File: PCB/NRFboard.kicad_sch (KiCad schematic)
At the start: 39 parts, among them J1 USB_C_Receptacle_USB2.0_14P, J2 Conn_01x20, J3 Conn_01x20, J4 Conn_01x03, J5 Conn_01x03, SW1 SW_Push, U2 MCP1700x-300xxTT, U4 nRF52840, U7 BQ24075RGT, Y1 32Mhz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

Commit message: updated routing, should be finalized and ready for production
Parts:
- added C10, C9: 10uF, Capacitor_SMD:C_0603_1608Metric, symbol Device:C
- added C11, C5: 1uF, Capacitor_SMD:C_0402_1005Metric, symbol Device:C
- added C4, C8: 0.1uF, Capacitor_SMD:C_0402_1005Metric, symbol Device:C
- added C6: 22uF, Capacitor_SMD:C_0805_2012Metric, symbol Device:C
- added D1: green, LED_SMD:LED_0805_2012Metric, symbol Device:LED
- added J6: Conn_01x02, Connector_JST:JST_PH_B2B-PH-K_1x02_P2.00mm_Vertical, symbol Connector_Generic:Conn_01x02
- added R4: 1.5k, Resistor_SMD:R_0402_1005Metric, symbol Device:R
- C18, C19: value 20pF -> 12pF
- C22, C25, C29: footprint Capacitor_SMD:C_0402_1005Metric -> Capacitor_SMD:C_0603_1608Metric
- C31, C32: value 15pF -> 12.5pF
- R11: value 10k -> 1.5k
- renumbered D89 to D2
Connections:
- net +3V3: now also C11.1, C9.1
- net GND: now also U7.6 (EN1), C10.1, C11.2, C4.2, C5.2, C6.2, C8.2, C9.2, J6.2 (Pin_2); no longer U7.5 (EN2)
- net Out: now also J3.20 (Pin_20), C10.2, C4.1, C5.1, C6.1, C8.1, R4.2
- net VBAT: now also U7.5 (EN2), J6.1 (Pin_1); no longer J3.20 (Pin_20), U7.6 (EN1)
- net at U7.7 (~{PGOOD}): now also D1.1 (K)
- new net: D1.2 (A), R4.1
- no-connect marks 14 -> 12
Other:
- note added: "VDD must be configured on regout0 to 5 to output 3v3, otherwise 1.8v default 3v3 needed to activate neopixel in current config since there's no vbus there's no need to set reg0"
- note removed: "VDD must be configured on regout0 to 5 to output 3v3, otherwise 1.8v default 3v3 needed to activate neopixel"
- moved on the sheet: U2

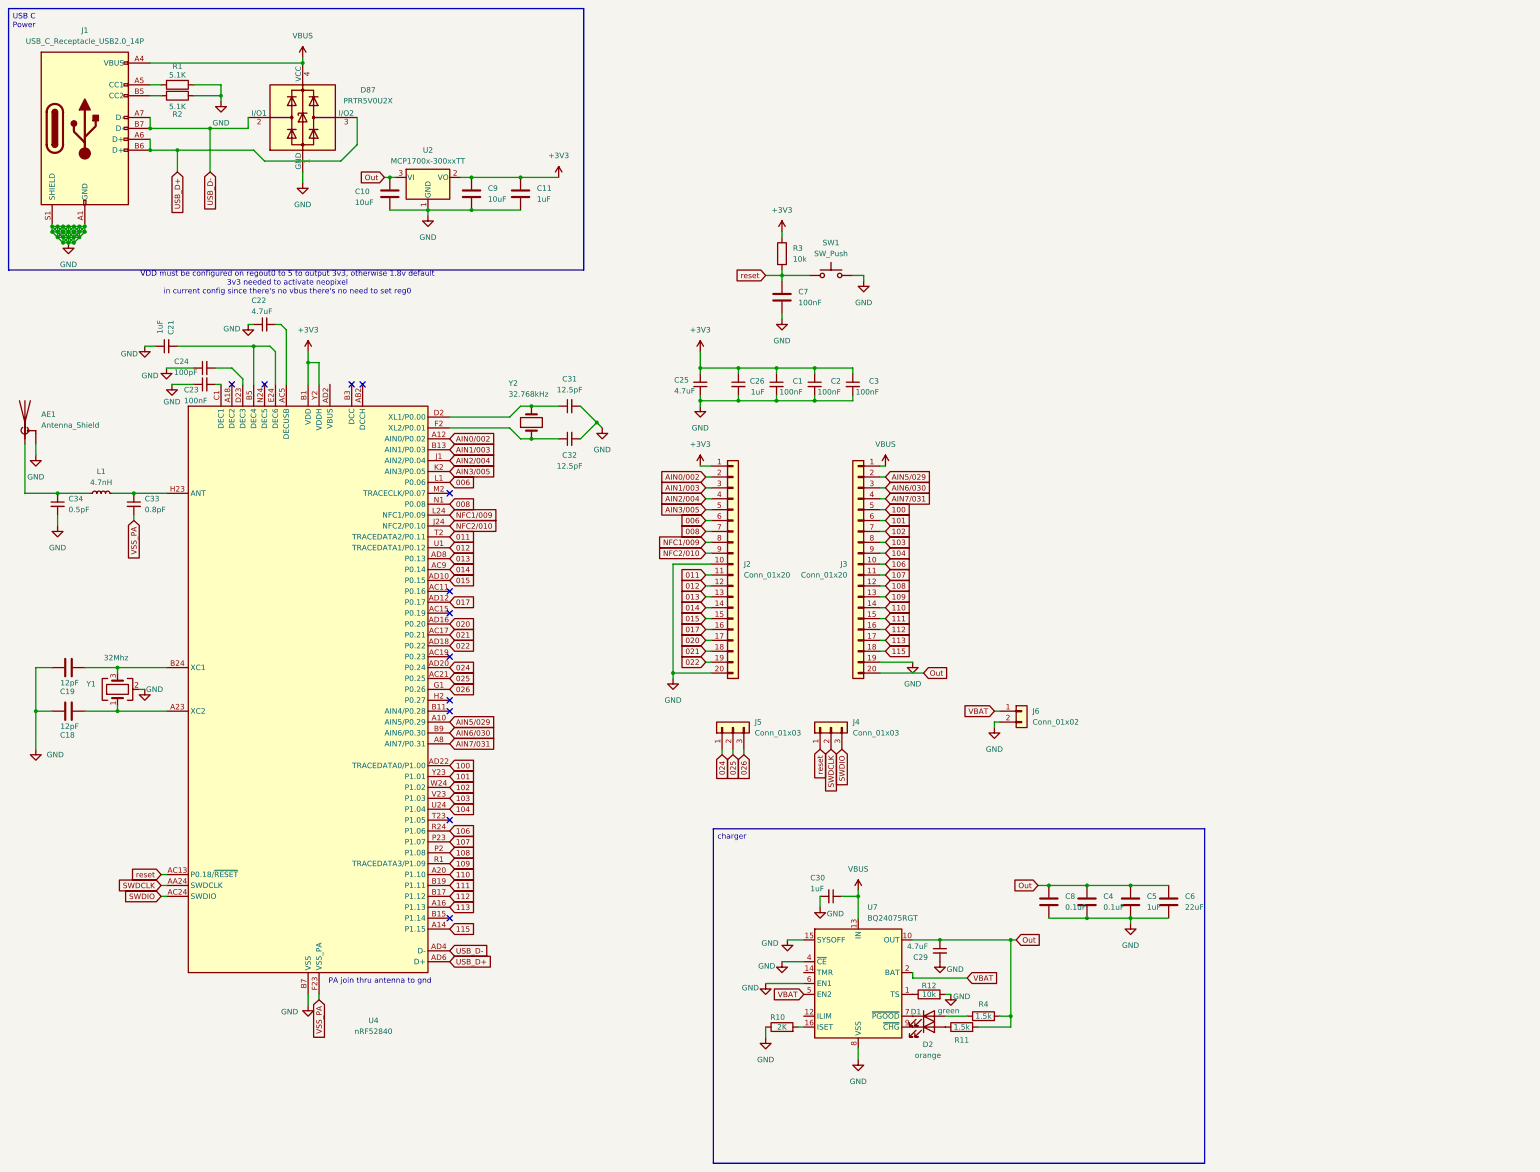
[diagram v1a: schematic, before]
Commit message: update rf, wanted to add qspi but reverted
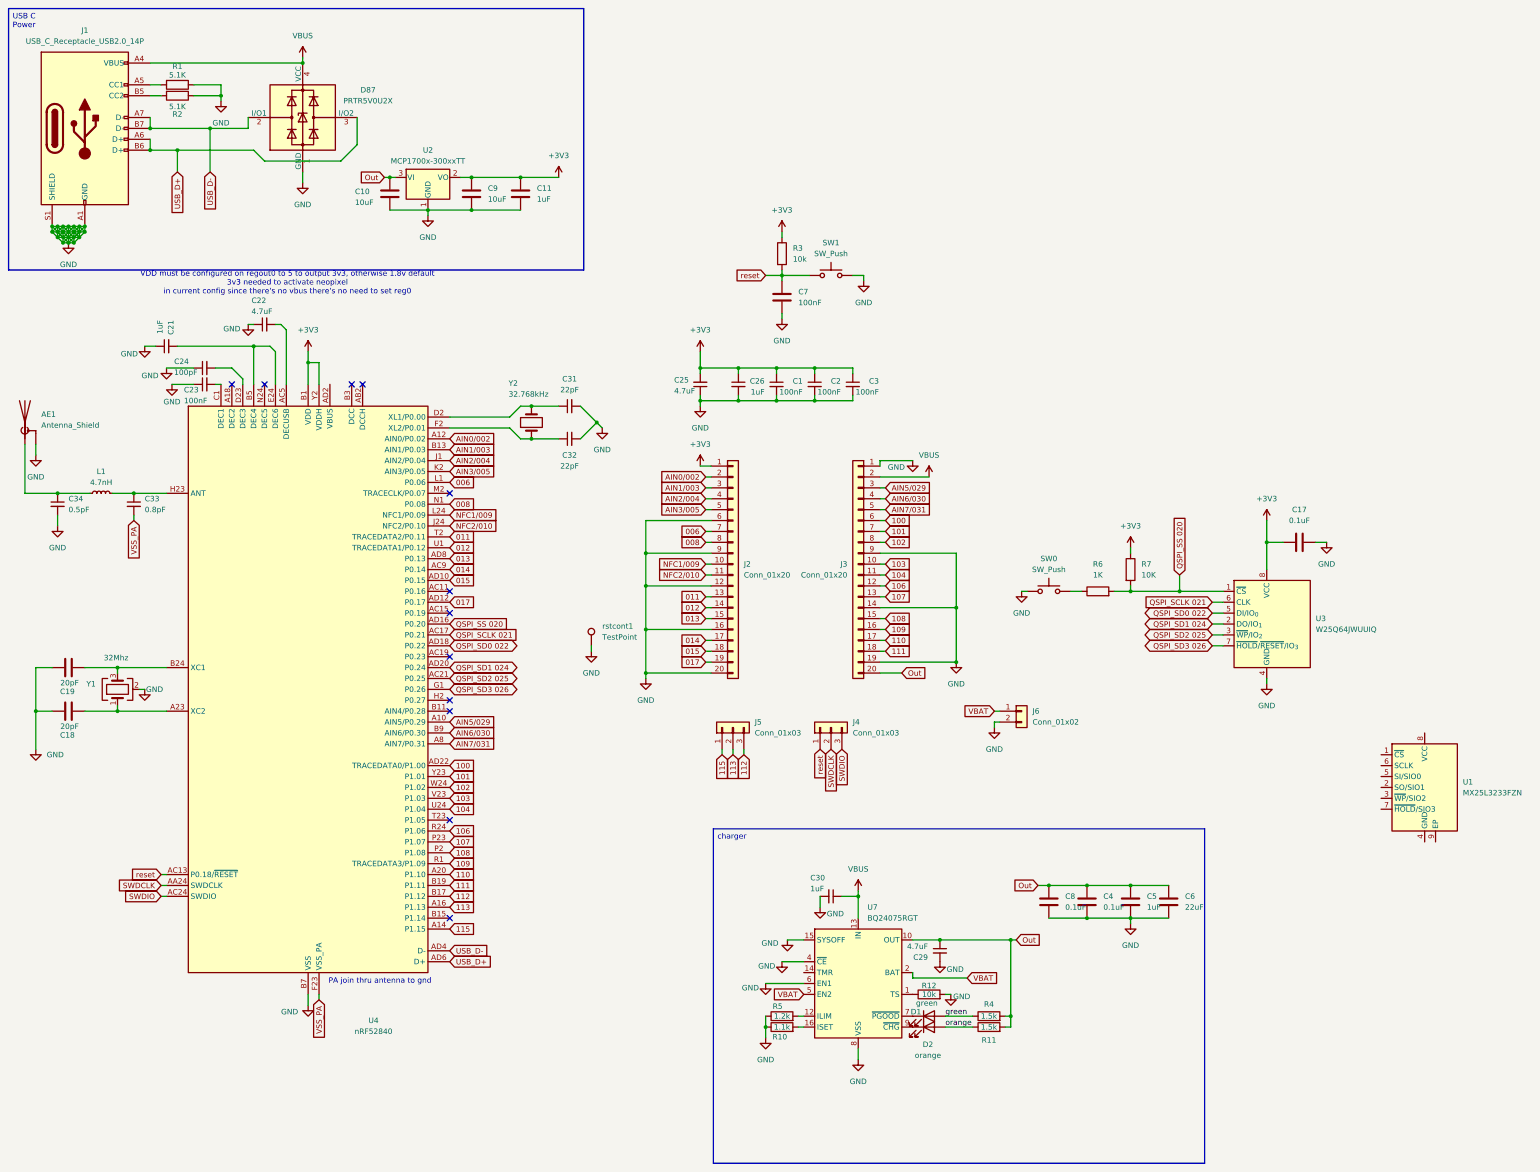
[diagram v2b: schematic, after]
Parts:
- added C17: 0.1uF, Capacitor_SMD:C_0402_1005Metric, symbol Device:C
- added R5: 1.2k, Resistor_SMD:R_0402_1005Metric, symbol Device:R
- added R6: 1K, Resistor_SMD:R_0402_1005Metric, symbol Device:R
- added R7: 10K, Resistor_SMD:R_0402_1005Metric, symbol Device:R
- added SW0: SW_Push, Button_Switch_SMD:SW_Push_SPST_NO_Alps_SKRK, symbol Switch:SW_Push
- added U1: MX25L3233FZN, Package_SON:WSON-8-1EP_6x5mm_P1.27mm_EP3.4x4.3mm, symbol Memory_Flash:MX25L3233FZN
- added U3: W25Q64JWUUIQ, Package_SON:Winbond_USON-8-1EP_3x2mm_P0.5mm_EP0.2x1.6mm, symbol Memory_Flash:W25Q128JVS
- added rstcont1: TestPoint, TestPoint:TestPoint_Pad_D1.0mm, symbol Connector:TestPoint
- C18, C19: value 12pF -> 20pF
- C31, C32: value 12.5pF -> 22pF
- R10: value 2K -> 1.1k
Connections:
- net +3V3: now also C17.1, R7.1, U3.8 (VCC)
- net 006: now also J2.7 (Pin_7); no longer J2.6 (Pin_6)
- net 008: now also J2.8 (Pin_8); no longer J2.7 (Pin_7)
- net 011: now also J2.13 (Pin_13); no longer J2.11 (Pin_11)
- net 012: now also J2.14 (Pin_14); no longer J2.12 (Pin_12)
- net 013: now also J2.15 (Pin_15); no longer J2.13 (Pin_13)
- net 014: now also J2.17 (Pin_17); no longer J2.14 (Pin_14)
- net 015: now also J2.18 (Pin_18); no longer J2.15 (Pin_15)
- net 017: now also J2.19 (Pin_19); no longer J2.16 (Pin_16)
- net 100: now also J3.6 (Pin_6); no longer J3.5 (Pin_5)
- net 101: now also J3.7 (Pin_7); no longer J3.6 (Pin_6)
- net 102: now also J3.8 (Pin_8); no longer J3.7 (Pin_7)
- net 103: now also J3.10 (Pin_10); no longer J3.8 (Pin_8)
- net 104: now also J3.11 (Pin_11); no longer J3.9 (Pin_9)
- net 106: now also J3.12 (Pin_12); no longer J3.10 (Pin_10)
- net 107: now also J3.13 (Pin_13); no longer J3.11 (Pin_11)
- net 108: now also J3.15 (Pin_15); no longer J3.12 (Pin_12)
- net 109: now also J3.16 (Pin_16); no longer J3.13 (Pin_13)
- net 110: now also J3.17 (Pin_17); no longer J3.14 (Pin_14)
- net 111: now also J3.18 (Pin_18); no longer J3.15 (Pin_15)
- net 112: now also J5.3 (Pin_3); no longer J3.16 (Pin_16)
- net 113: now also J5.2 (Pin_2); no longer J3.17 (Pin_17)
- net 115: now also J5.1 (Pin_1); no longer J3.18 (Pin_18)
- net AIN5/029: now also J3.3 (Pin_3); no longer J3.2 (Pin_2)
- net AIN6/030: now also J3.4 (Pin_4); no longer J3.3 (Pin_3)
- net AIN7/031: now also J3.5 (Pin_5); no longer J3.4 (Pin_4)
- net GND: now also J2.12 (Pin_12), J2.16 (Pin_16), J2.6 (Pin_6), J2.9 (Pin_9), J3.1 (Pin_1), J3.14 (Pin_14), J3.9 (Pin_9), C17.2, R5.1, SW0.1, U3.4 (GND), rstcont1.1; no longer J2.10 (Pin_10)
- net NFC1/009: now also J2.10 (Pin_10); no longer J2.8 (Pin_8)
- net NFC2/010: now also J2.11 (Pin_11); no longer J2.9 (Pin_9)
- net VBUS: now also J3.2 (Pin_2); no longer J3.1 (Pin_1)
- net green: now reaches D1.2 (A), R4.1
- net orange: now reaches D2.2 (A), R11.1
- net at U7.12 (ILIM): now also R5.2
- net 020 renamed QSPI_SS 020
- net QSPI_SS 020: now also R6.2, R7.2, U3.1 (~{CS}); no longer J2.17 (Pin_17)
- net 021 renamed QSPI_SCLK 021
- net QSPI_SCLK 021: now also U3.6 (CLK); no longer J2.18 (Pin_18)
- net 022 renamed QSPI_SD0 022
- net QSPI_SD0 022: now also U3.5 (DI/IO_{0}); no longer J2.19 (Pin_19)
- net 024 renamed QSPI_SD1 024
- net QSPI_SD1 024: now also U3.2 (DO/IO_{1}); no longer J5.1 (Pin_1)
- net 025 renamed QSPI_SD2 025
- net QSPI_SD2 025: now also U3.3 (~{WP}/IO_{2}); no longer J5.2 (Pin_2)
- net 026 renamed QSPI_SD3 026
- net QSPI_SD3 026: now also U3.7 (~{HOLD}/~{RESET}/IO_{3}); no longer J5.3 (Pin_3)
- new net: R6.1, SW0.2
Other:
- moved on the sheet: R11, R4

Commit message: updated layout, added more vias, matched impedance for usb line for a coplanar diff
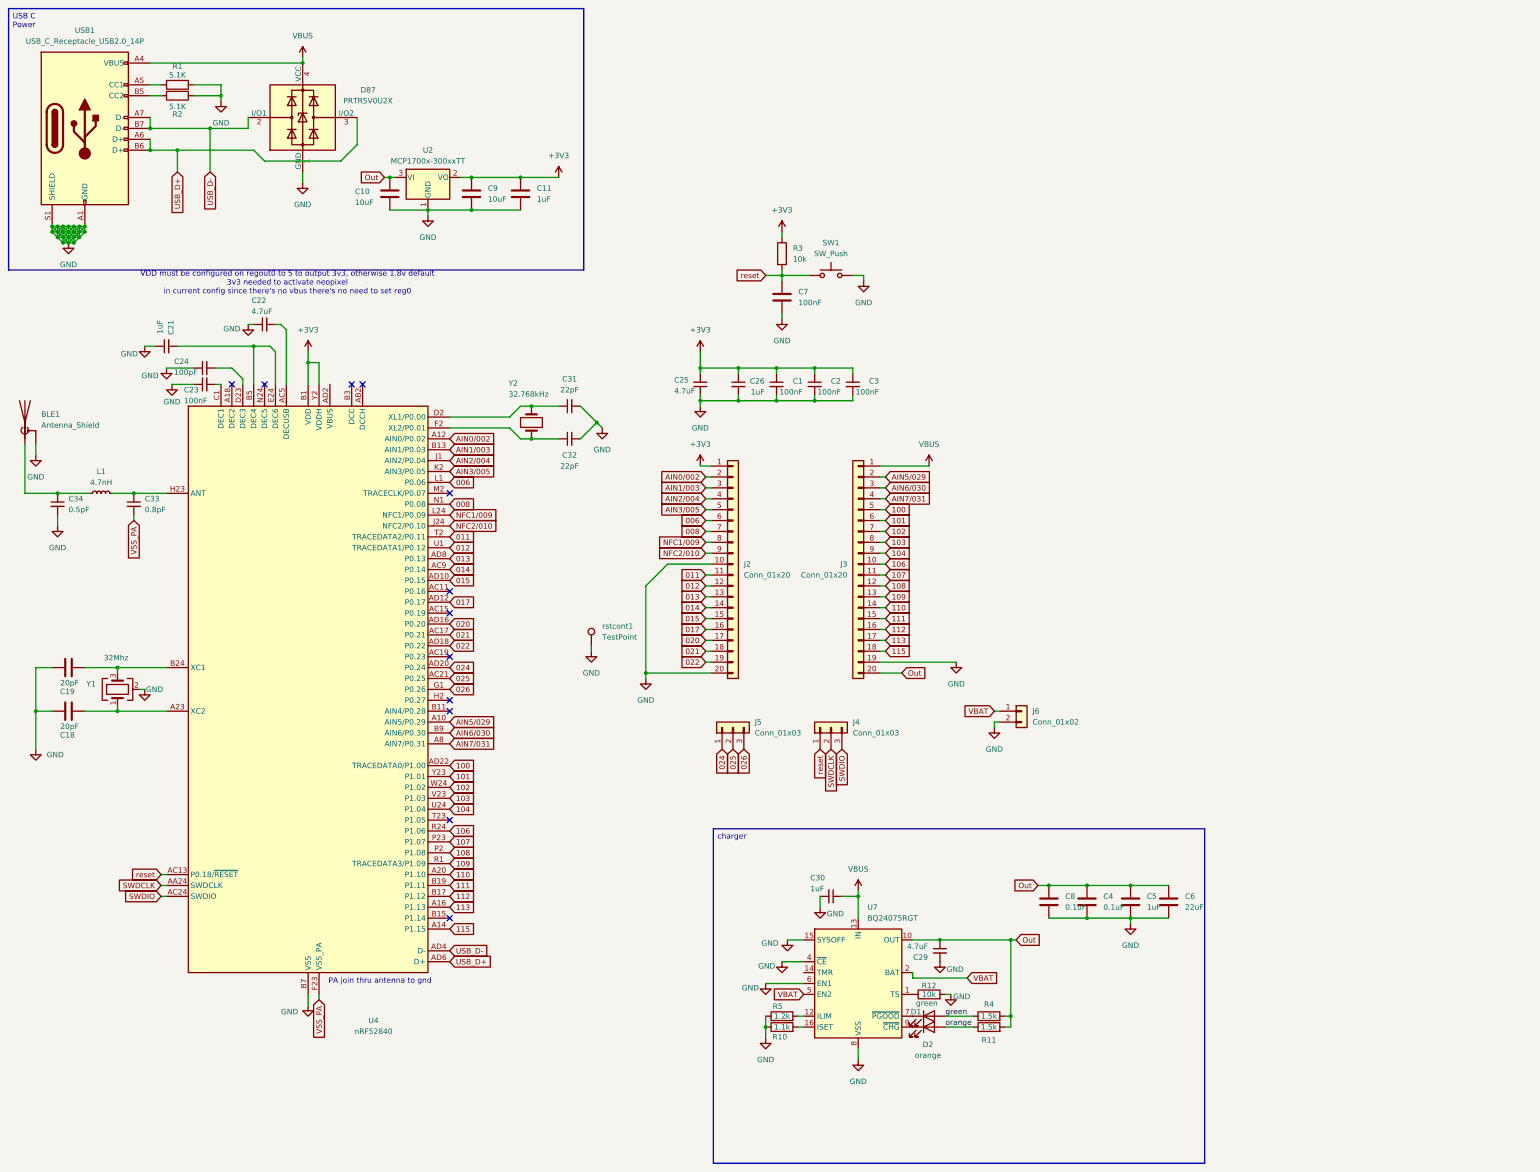
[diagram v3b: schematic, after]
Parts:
- removed C17: 0.1uF, Capacitor_SMD:C_0402_1005Metric, symbol Device:C
- removed R6: 1K, Resistor_SMD:R_0402_1005Metric, symbol Device:R
- removed R7: 10K, Resistor_SMD:R_0402_1005Metric, symbol Device:R
- removed SW0: SW_Push, Button_Switch_SMD:SW_Push_SPST_NO_Alps_SKRK, symbol Switch:SW_Push
- removed U1: MX25L3233FZN, Package_SON:WSON-8-1EP_6x5mm_P1.27mm_EP3.4x4.3mm, symbol Memory_Flash:MX25L3233FZN
- removed U3: W25Q64JWUUIQ, Package_SON:Winbond_USON-8-1EP_3x2mm_P0.5mm_EP0.2x1.6mm, symbol Memory_Flash:W25Q128JVS
- renumbered AE1 to BLE1, J1 to USB1
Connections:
- net 006: now also J2.6 (Pin_6); no longer J2.7 (Pin_7)
- net 008: now also J2.7 (Pin_7); no longer J2.8 (Pin_8)
- net 011: now also J2.11 (Pin_11); no longer J2.13 (Pin_13)
- net 012: now also J2.12 (Pin_12); no longer J2.14 (Pin_14)
- net 013: now also J2.13 (Pin_13); no longer J2.15 (Pin_15)
- net 014: now also J2.14 (Pin_14); no longer J2.17 (Pin_17)
- net 015: now also J2.15 (Pin_15); no longer J2.18 (Pin_18)
- net 017: now also J2.16 (Pin_16); no longer J2.19 (Pin_19)
- net 100: now also J3.5 (Pin_5); no longer J3.6 (Pin_6)
- net 101: now also J3.6 (Pin_6); no longer J3.7 (Pin_7)
- net 102: now also J3.7 (Pin_7); no longer J3.8 (Pin_8)
- net 103: now also J3.8 (Pin_8); no longer J3.10 (Pin_10)
- net 104: now also J3.9 (Pin_9); no longer J3.11 (Pin_11)
- net 106: now also J3.10 (Pin_10); no longer J3.12 (Pin_12)
- net 107: now also J3.11 (Pin_11); no longer J3.13 (Pin_13)
- net 108: now also J3.12 (Pin_12); no longer J3.15 (Pin_15)
- net 109: now also J3.13 (Pin_13); no longer J3.16 (Pin_16)
- net 110: now also J3.14 (Pin_14); no longer J3.17 (Pin_17)
- net 111: now also J3.15 (Pin_15); no longer J3.18 (Pin_18)
- net 112: now also J3.16 (Pin_16); no longer J5.3 (Pin_3)
- net 113: now also J3.17 (Pin_17); no longer J5.2 (Pin_2)
- net 115: now also J3.18 (Pin_18); no longer J5.1 (Pin_1)
- net AIN5/029: now also J3.2 (Pin_2); no longer J3.3 (Pin_3)
- net AIN6/030: now also J3.3 (Pin_3); no longer J3.4 (Pin_4)
- net AIN7/031: now also J3.4 (Pin_4); no longer J3.5 (Pin_5)
- net GND: now also J2.10 (Pin_10); no longer J2.12 (Pin_12), J2.16 (Pin_16), J2.6 (Pin_6), J2.9 (Pin_9), J3.1 (Pin_1), J3.14 (Pin_14), J3.9 (Pin_9)
- net NFC1/009: now also J2.8 (Pin_8); no longer J2.10 (Pin_10)
- net NFC2/010: now also J2.9 (Pin_9); no longer J2.11 (Pin_11)
- net VBUS: now also J3.1 (Pin_1); no longer J3.2 (Pin_2)
- net QSPI_SCLK 021 renamed 021
- net 021: now also J2.18 (Pin_18)
- net QSPI_SD0 022 renamed 022
- net 022: now also J2.19 (Pin_19)
- net QSPI_SD1 024 renamed 024
- net 024: now also J5.1 (Pin_1)
- net QSPI_SD2 025 renamed 025
- net 025: now also J5.2 (Pin_2)
- net QSPI_SD3 026 renamed 026
- net 026: now also J5.3 (Pin_3)
- net QSPI_SS 020 renamed 020
- net 020: now also J2.17 (Pin_17)
